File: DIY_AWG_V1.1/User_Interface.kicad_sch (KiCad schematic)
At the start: 33 parts, among them SW10 SW_Push, SW11 SW_Push, SW12 SW_Push, SW13 SW_Push, SW14 SW_Push, SW15 SW_Push, SW16 SW_Push, SW17 SW_Push, SW18 SW_Push, SW19 SW_Push, SW20 SW_Push, SW21 SW_Push, SW22 SW_Push, SW23 SW_Push, SW3 SW_Push, SW4 SW_Push, SW5 SW_Push, SW6 SW_Push, SW7 SW_Push, SW8 SW_Push, SW9 SW_Push, U14 EC12D1564402, U15 EC12E2430404

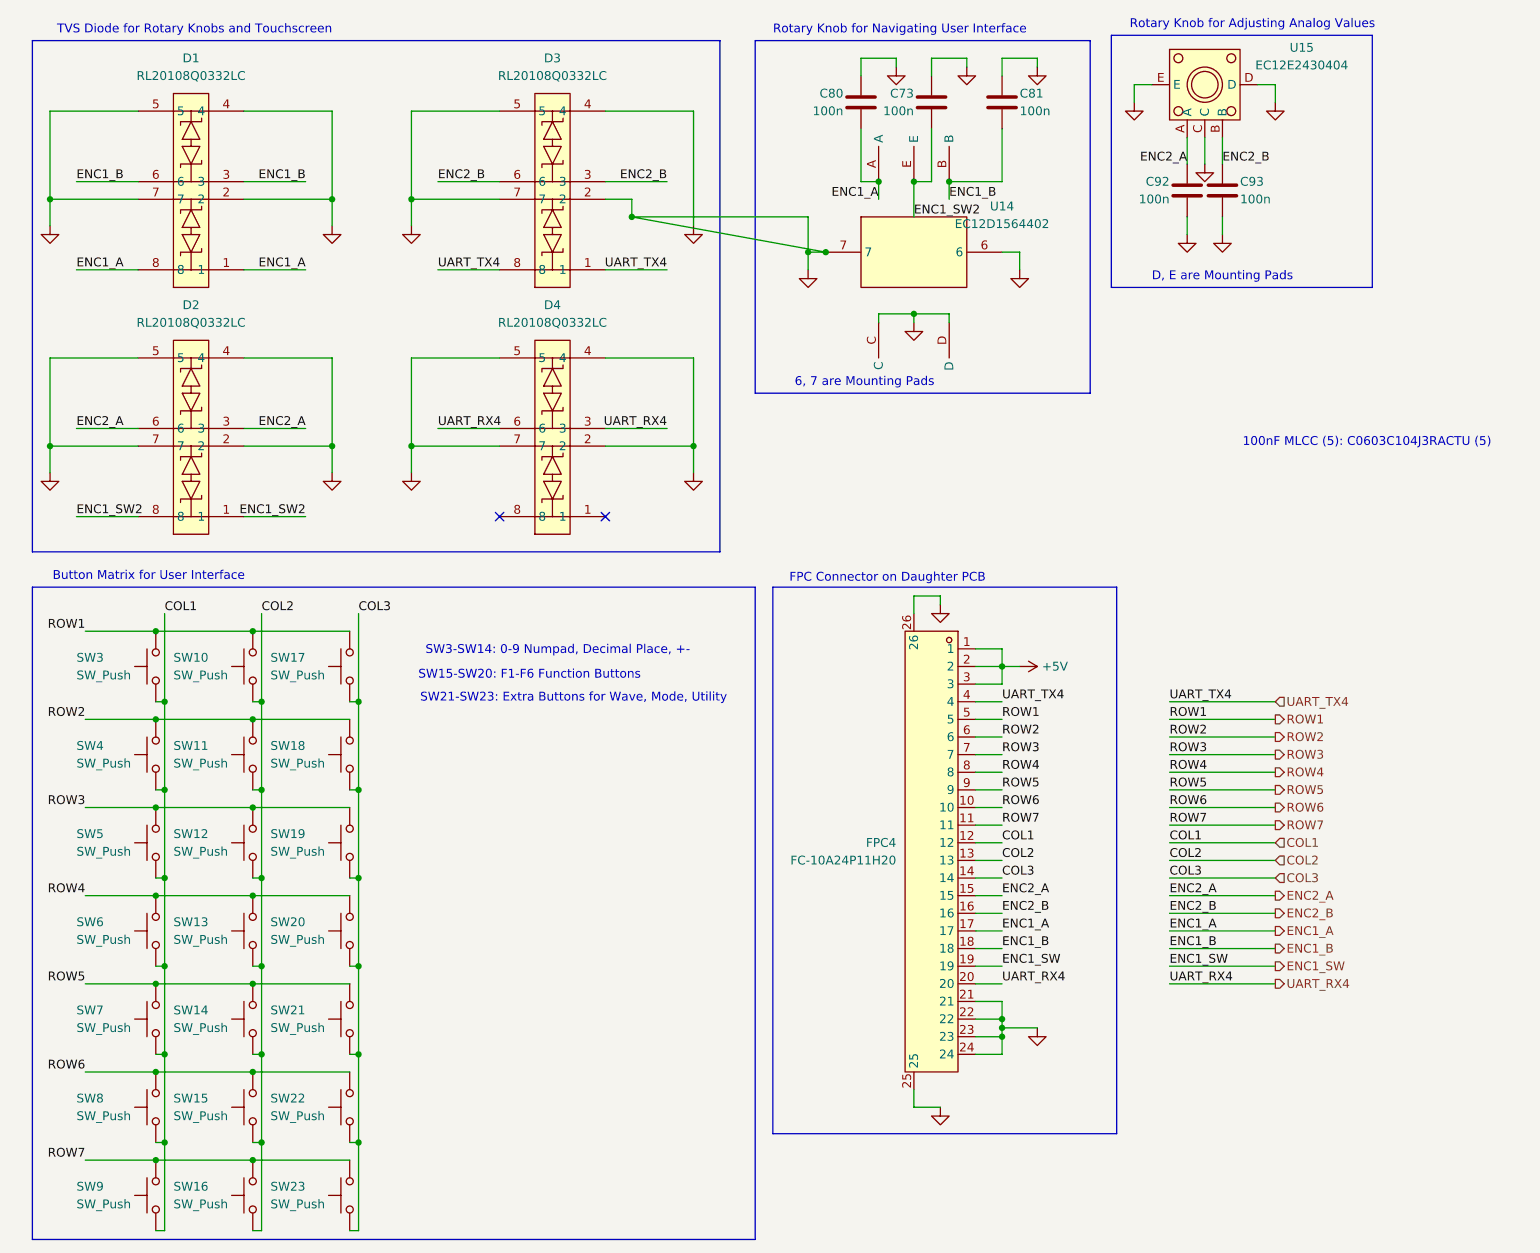
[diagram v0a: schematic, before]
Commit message: Updated component footprints
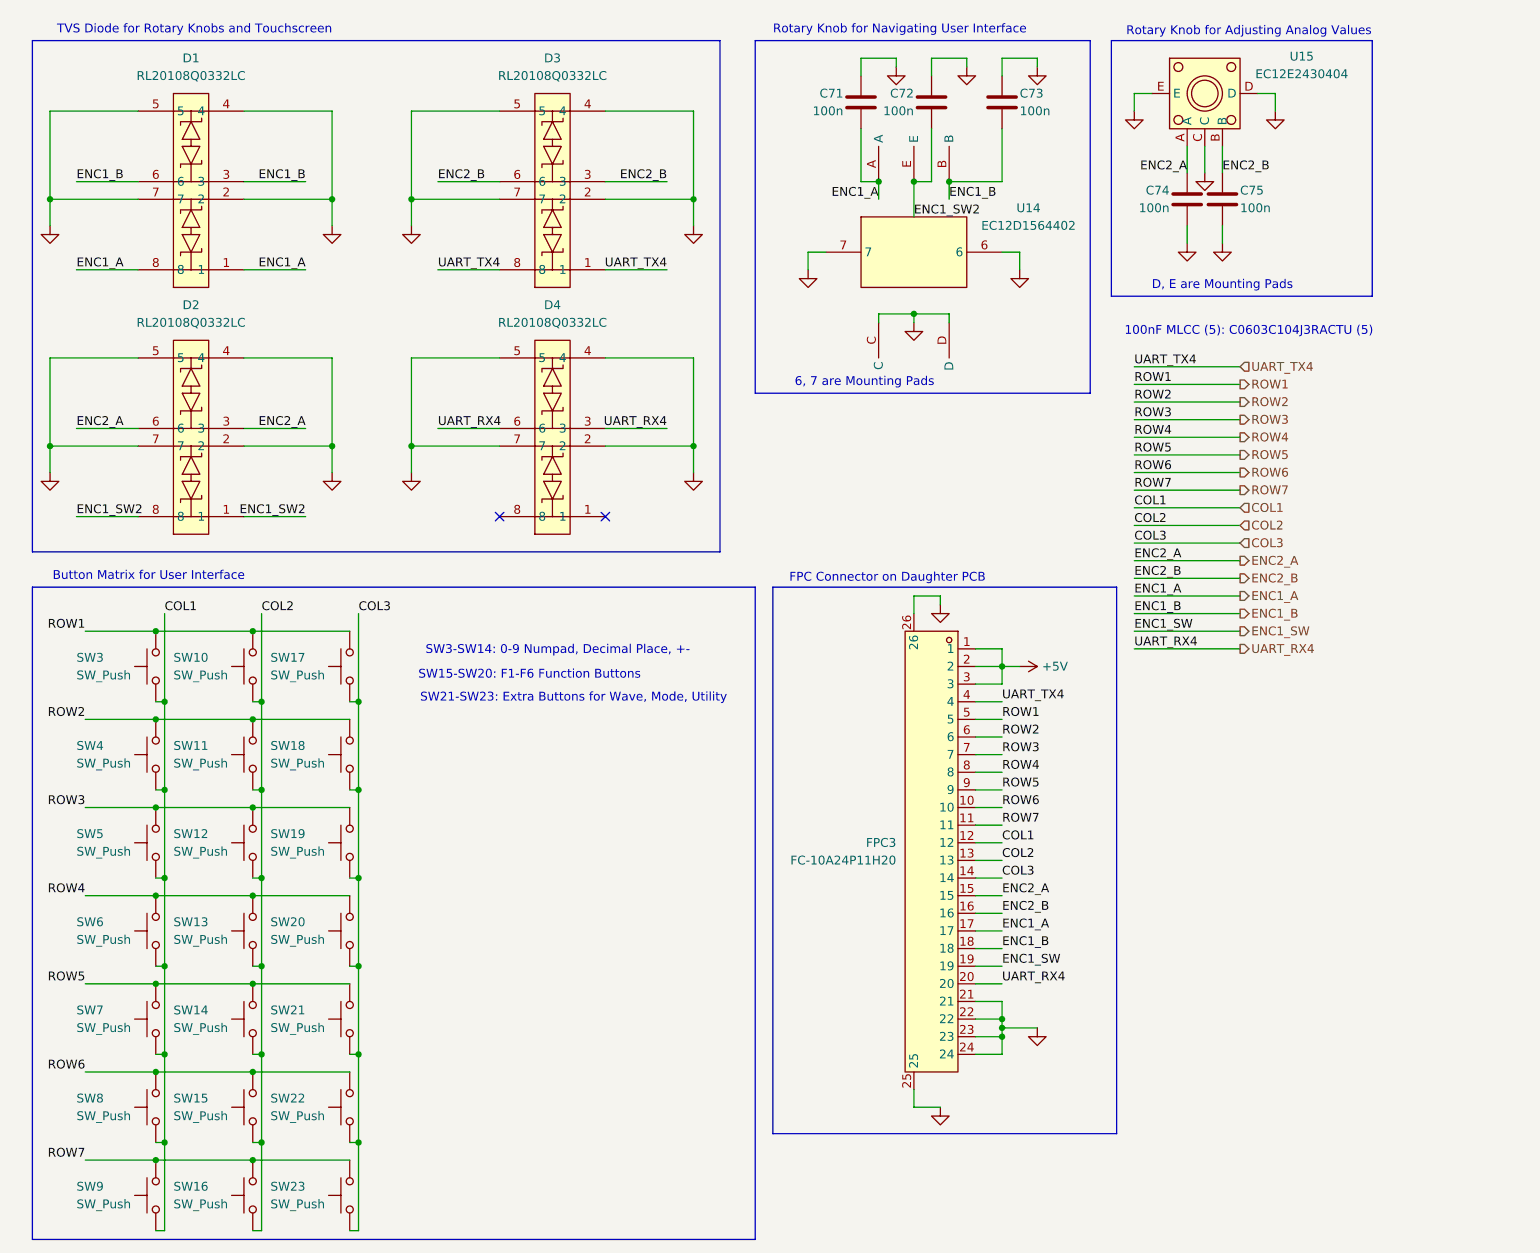
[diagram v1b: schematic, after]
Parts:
- renumbered C80 to C71, C73 to C72, C81 to C73, C92 to C74, C93 to C75, FPC4 to FPC3
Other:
- moved on the sheet: C74, C75, U15

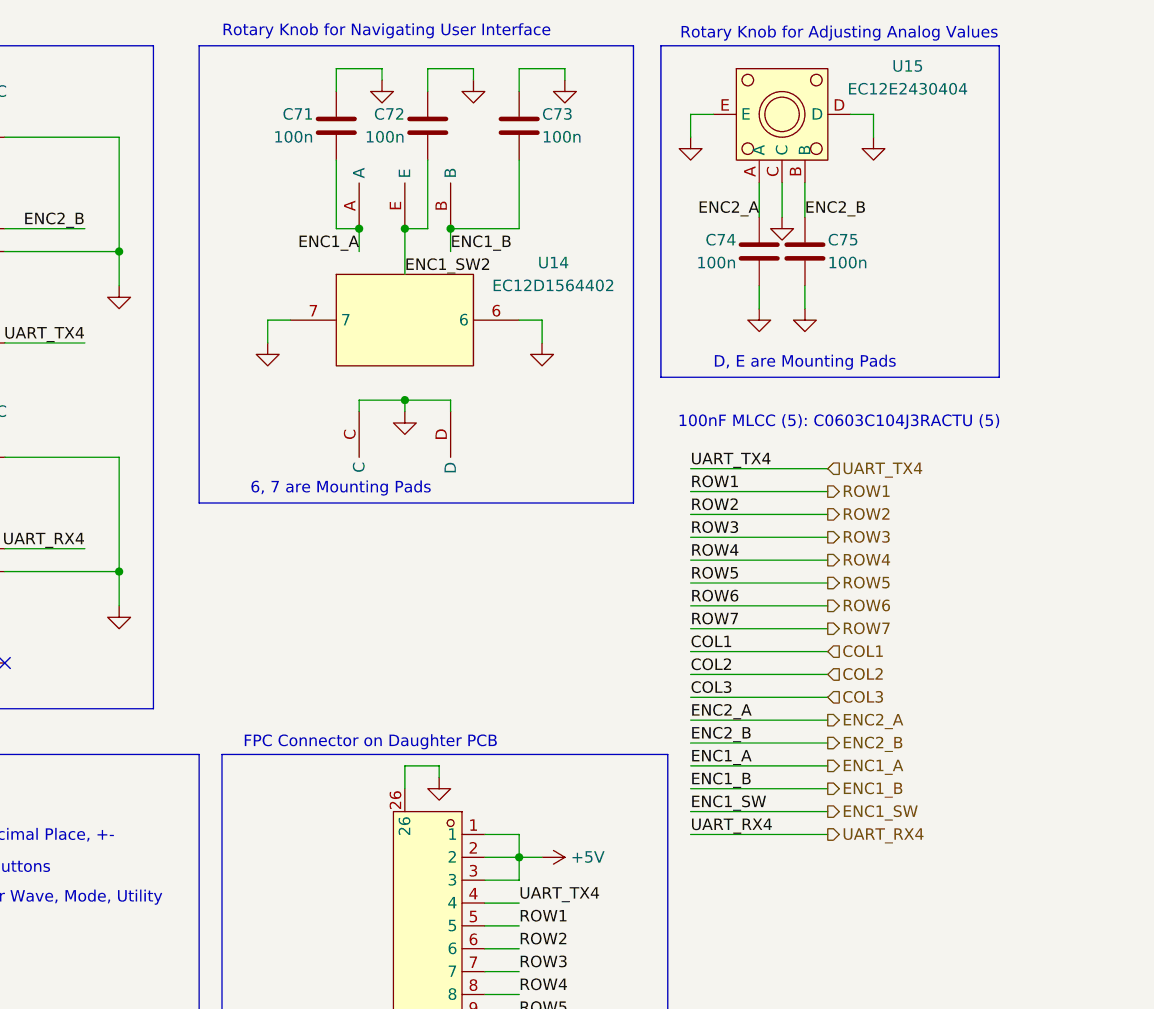
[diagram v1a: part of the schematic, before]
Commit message: Updated component footprints
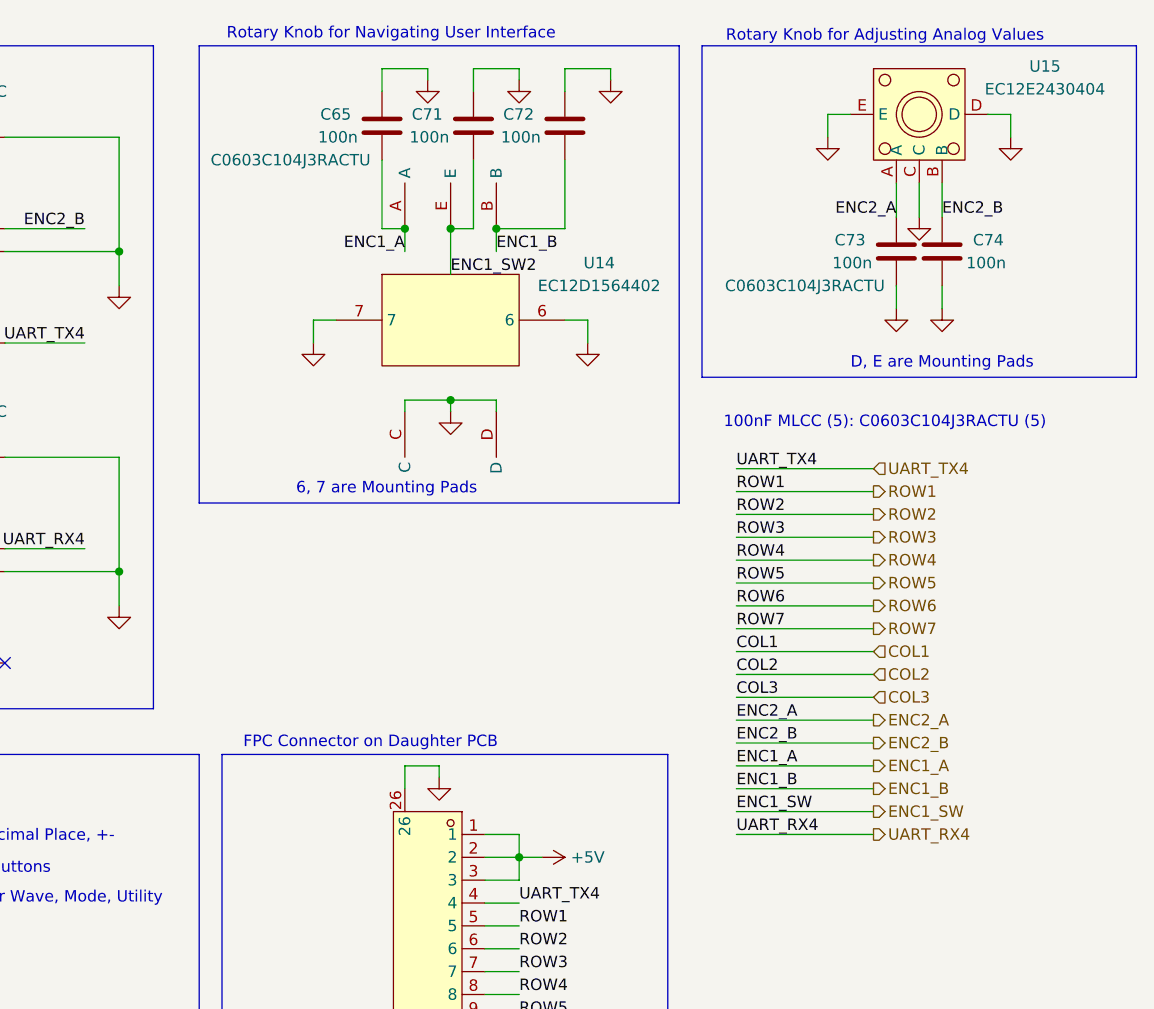
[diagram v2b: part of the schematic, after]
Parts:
- removed C75: 100n, symbol Device:C
- added C65: 100n, Capacitor_SMD:C_0603_1608Metric, symbol Device:C
- C71, C72, C73, C74: footprint (none) -> Capacitor_SMD:C_0603_1608Metric; Component Name (none) -> C0603C104J3RACTU; LCSC ID (none) -> C2167388
- SW10, SW11, SW12, SW13, SW14, SW15, SW16, SW17, SW18, SW19, SW20, SW21, SW22, SW23, SW3, SW4, SW5, SW6, SW7, SW8, SW9: footprint (none) -> easyeda2kicad:SW-SMD_L6.1-W3.5-LS8.6
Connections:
- net ENC1_A: now also C65.1; no longer C71.2
- net ENC1_B: now also C72.1; no longer C73.2
- net ENC1_SW2: now also C71.1; no longer C72.2
- net ENC2_A: now also C73.2; no longer C74.1
- net ENC2_B: now also C74.2
- net GND: now also C71.2, C72.2, C74.1, C65.2; no longer C71.1, C72.1, C74.2
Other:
- moved on the sheet: U14, U15

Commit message: Updated schematics
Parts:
- renumbered C65 to C71, C71 to C72, C72 to C73, C73 to C74, C74 to C75
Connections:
- net +5V renamed +VSW5V0

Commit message: Updated PCB design, uploaded necessary footprints and symbols for some components
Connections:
- net +VSW5V0 renamed +3V3
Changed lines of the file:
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@@
 	)
 	(symbol
+		(lib_id "power:+3V3")
+		(at 160.02 107.95 270)
+		(unit 1)
+		(body_style 1)
+		(exclude_from_sim no)
+		(in_bom yes)
+		(on_board yes)
+		(in_pos_files yes)
+		(dnp no)
+		(fields_autoplaced yes)
+		(property "Reference" "#PWR0176"
+			(at 156.21 107.95 0)
+			(hide yes)
+			(show_name no)
+			(do_not_autoplace no)
+			(effects
+				(font
+					(size 1.27 1.27)
+				)
+			)
+		)
+		(property "Value" "+3V3"
+			(at 163.83 107.9499 90)
+			(show_name no)
+			(do_not_autoplace no)
+			(effects
+				(font
+					(size 1.27 1.27)
+				)
+				(justify left)
+			)
+		)
+		(property "Footprint" ""
+			(at 160.02 107.95 0)
+			(hide yes)
+			(show_name no)
+			(do_not_autoplace no)
+			(effects
+				(font
+					(size 1.27 1.27)
+				)
+			)
+		)
+		(property "Datasheet" ""
+			(at 160.02 107.95 0)
+			(hide yes)
+			(show_name no)
+			(do_not_autoplace no)
+			(effects
+				(font
+					(size 1.27 1.27)
+				)
+			)
+		)
+		(property "Description" "Power symbol creates a global label with name \"+3V3\""
+			(at 160.02 107.95 0)
+			(hide yes)
+			(show_name no)
+			(do_not_autoplace no)
+			(effects
+				(font
+					(size 1.27 1.27)
+				)
+			)
+		)
+		(pin "1"
+		)
+		(instances
+			(project "DIY_AWG_V1.1"
+				(path "/508078af-d961-4af3-840e-a064a9f8d5bc/5e4867af-4e97-464f-8d5d-dfa2d7b207c5"
+					(reference "#PWR0176")
+					(unit 1)
+				)
+			)
+		)
+	)
+	(symbol
 		(lib_id "power:GND")
 		(at 167.64 21.59 0)
@@
 					(unit 1)
 				)
-			)
-		)
-	)
-	(symbol
-		(lib_id "power:+VSW")
-		(at 160.02 107.95 270)
-		(unit 1)
-		(body_style 1)
-		(exclude_from_sim no)
-		(in_bom yes)
-		(on_board yes)
-		(in_pos_files yes)
-		(dnp no)
-		(fields_autoplaced yes)
-		(property "Reference" "#PWR0176"
-			(at 156.21 107.95 0)
-			(hide yes)
-			(show_name no)
-			(do_not_autoplace no)
-			(effects
-				(font
-					(size 1.27 1.27)
-				)
-			)
-		)
-		(property "Value" "+VSW5V0"
-			(at 163.83 107.9499 90)
-			(show_name no)
-			(do_not_autoplace no)
-			(effects
-				(font
-					(size 1.27 1.27)
-				)
-				(justify left)
-			)
-		)
-		(property "Footprint" ""
-			(at 160.02 107.95 0)
-			(hide yes)
-			(show_name no)
-			(do_not_autoplace no)
-			(effects
-				(font
-					(size 1.27 1.27)
-				)
-			)
-		)
-		(property "Datasheet" ""
-			(at 160.02 107.95 0)
-			(hide yes)
-			(show_name no)
-			(do_not_autoplace no)
-			(effects
-				(font
-					(size 1.27 1.27)
-				)
-			)
-		)
-		(property "Description" "Power symbol creates a global label with name \"+VSW\""
-			(at 160.02 107.95 0)
-			(hide yes)
-			(show_name no)
-			(do_not_autoplace no)
-			(effects
-				(font
-					(size 1.27 1.27)
-				)
-			)
-		)
-		(pin "1"
-		)
-		(instances
-			(project "DIY_AWG_V1.1"
-				(path "/508078af-d961-4af3-840e-a064a9f8d5bc/5e4867af-4e97-464f-8d5d-dfa2d7b207c5"
-					(reference "#PWR0176")
-					(unit 1)
-				)
